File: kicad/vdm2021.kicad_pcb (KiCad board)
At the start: 2 copper layers, 254 x 134.1 mm, 177 parts, among them IC1 7406, IC10 74LS109, IC11 74LS138, IC12 74LS86, IC13 74LS109, IC14 74LS02, IC15 74LS00, IC16 74LS109, IC17 74LS175, IC18 74LS132, IC19 74LS04, IC2 74LS163, IC20 74LS163, IC21 74LS163, IC22 74LS163, IC23 74LS157, IC24 74LS157, IC25 4049, IC26 4029, IC27 4029, IC28 74LS157, IC29 DM8131, IC3 74166, IC30 4001, IC31 4042, IC32 4042, IC33 74LS08, IC34 74LS08, IC35 74LS00, IC36 74LS04, IC37 8836, IC38 74LS367, IC39 74LS367, IC4 MCM6575, IC40 74LS10, IC41 2102, IC42 2102, IC43 2102, IC44 2102, IC45 2102, IC46 2102, IC47 2102, IC48 2102, IC49 L7805, IC5 74LS175, IC50 L7812, IC6 74LS175, IC7 74LS20, IC8 93L16, IC9 74LS10, J2 Jumper_3_Open, J4 Jumper_2_Open, J5 Jumper_2_Open, Q1 2N2907, SW1 SW_DIP_x06, Y1 Crystal

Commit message: Cleanup structure
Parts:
- ADDR1: footprint vdm2:ADDR_SELECT -> vdm2021:ADDR_SELECT
- HEAT: footprint vdm2:heatsink -> vdm2021:heatsink
- IC49: footprint vdm2:TO-220-3_Horizontal_TabDown -> vdm2021:TO-220-3_Horizontal_TabDown
- S100: footprint vdm2:S100_MALE -> vdm2021:S100_MALE
- VIDEO1: footprint vdm2:bnc-5-16345033 -> vdm2021:bnc-5-16345033
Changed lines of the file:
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@@
       (drillshape 0)
       (scaleselection 1)
-      (outputdirectory "/home/rob/Downloads/vdm2021"))
+      (outputdirectory ""))
   )
   (net 0 "")
@@
     (add_net "Net-(S100-Pad9)")
   )
-  (module vdm2:S100_MALE (layer F.Cu)
+  (module vdm2021:S100_MALE (layer F.Cu)
     (at 55.4482 151.9936)
     (descr "Connecteur Bus PC 8 bits")
@@
     )
   )
-  (module vdm2:TO-220-3_Horizontal_TabDown (layer F.Cu)
+  (module vdm2021:TO-220-3_Horizontal_TabDown (layer F.Cu)
     (at 47.625 58.57)
     (descr "TO-220-3, Horizontal, RM 2.54mm, see https://www.vishay.com/docs/66542/to-220-1.pdf")
@@
     )
   )
-  (module vdm2:bnc-5-16345033 locked (layer F.Cu)
+  (module vdm2021:bnc-5-16345033 locked (layer F.Cu)
     (at 261.62 34.925 270)
     (descr 5-1634503-3-1)
@@
     )
   )
-  (module vdm2:heatsink (layer F.Cu)
+  (module vdm2021:heatsink (layer F.Cu)
     (at 50.165 36.945)
     (fp_text reference HEAT (at 0 0.5) (layer F.SilkS) hide
@@
     )
   )
-  (module vdm2:ADDR_SELECT (layer F.Cu)
+  (module vdm2021:ADDR_SELECT (layer F.Cu)
     (at 101.219 117.094)
     (fp_text reference ADDR1 (at 0.7874 -4.0894) (layer F.SilkS) hide

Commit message: Routing updates after last schematic change
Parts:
- moved R46 3.79 mm to (145.1, 117.0)
- moved C41 0.90 mm to (200.3, 99.1)
- moved C11 0.08 mm to (142.0, 117.0)
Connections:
- IC29 pad 9: Net-(ADDR1-Pad13) -> Net-(IC29-Pad9)
- IC36 pad 3: Net-(ADDR1-Pad13) -> Net-(IC29-Pad9)
- IC37 pad 5: Net-(ADDR1-Pad13) -> Net-(IC29-Pad9)
- IC38 pad 15: Net-(ADDR1-Pad13) -> Net-(IC29-Pad9)
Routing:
- net Net-(IC31-Pad4): track 366.2 -> 180.4 mm, vias 6 -> 3
- net Net-(IC29-Pad9): track 0.00 -> 120.4 mm, vias 0 -> 2
- net Net-(ADDR1-Pad13): track 229.8 -> 284.0 mm
- net Net-(ADDR1-Pad10): track 153.9 -> 133.0 mm, vias 3 -> 2
- net Net-(IC32-Pad13): track 243.4 -> 222.9 mm
- net +5V: track 1752.7 -> 1743.2 mm
- net Net-(IC36-Pad1): track 92.7 -> 99.6 mm, vias 3 -> 2
- net Net-(IC38-Pad5): track 43.5 -> 49.8 mm, vias 2 -> 3
- net Net-(IC29-Pad13): track 61.6 -> 67.1 mm
- net Net-(IC29-Pad3): track 76.4 -> 81.7 mm
- net Net-(IC29-Pad5): track 75.7 -> 80.8 mm
- net Net-(IC28-Pad6): track 116.7 -> 112.9 mm
- net Net-(IC33-Pad5): track 59.6 -> 63.3 mm
- net Net-(IC36-Pad8): track 114.8 -> 117.8 mm, vias 1 -> 2
- net Net-(IC34-Pad1): track 78.0 -> 75.4 mm
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
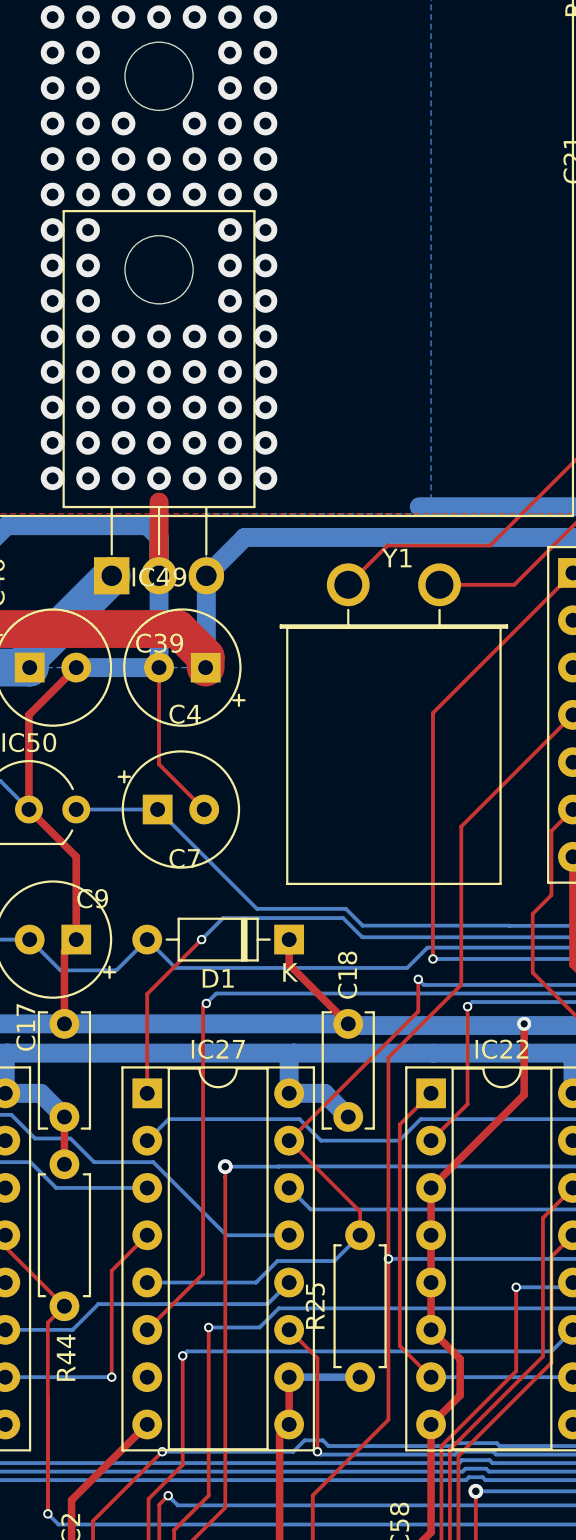
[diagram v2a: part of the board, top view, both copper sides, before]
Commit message: Fixed IC22 load value
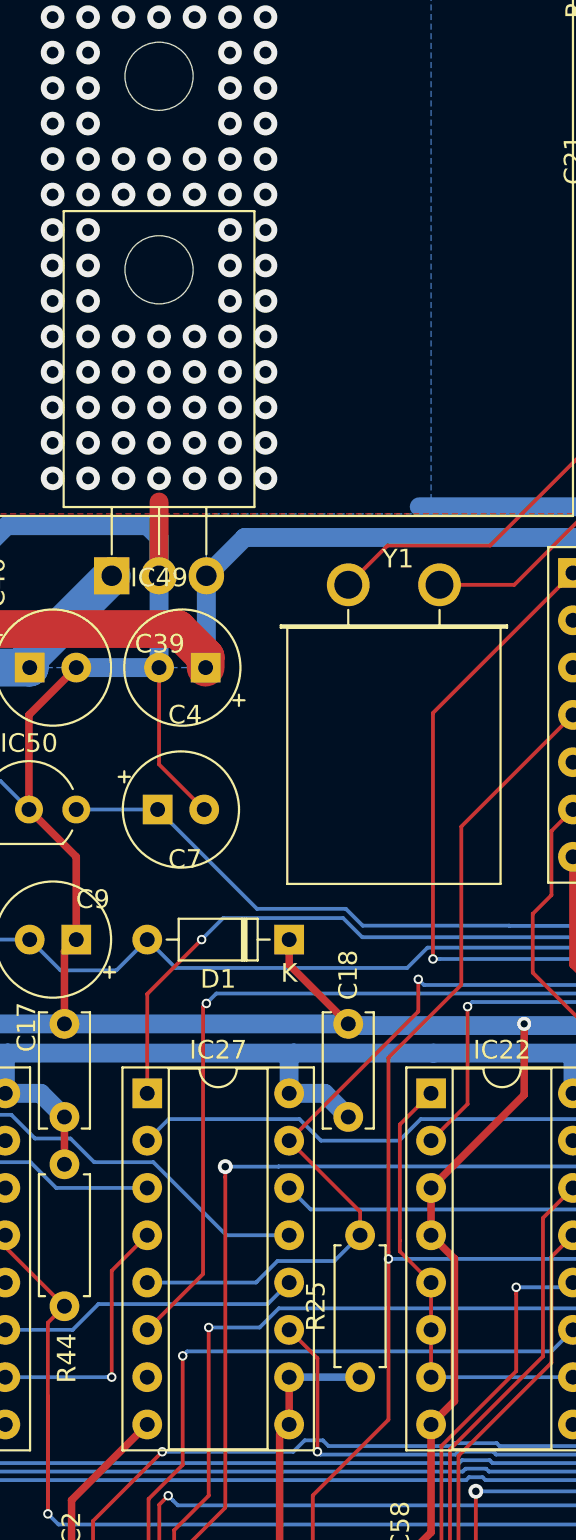
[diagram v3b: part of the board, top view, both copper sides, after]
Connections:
- IC22 pad 5: GND -> Net-(IC20-Pad1)
- IC22 pad 6: GND -> Net-(IC20-Pad1)
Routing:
- net GND: track 2507.7 -> 2507.5 mm, vias 142 -> 140

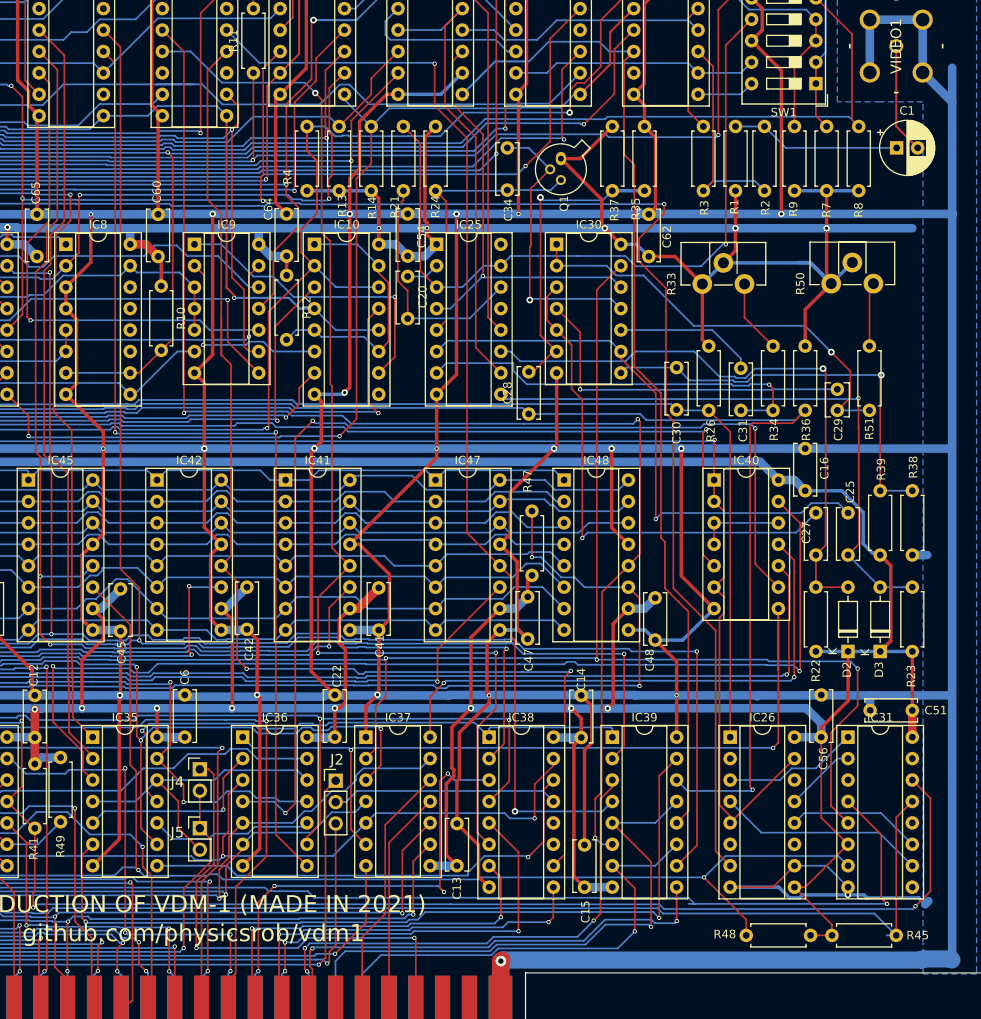
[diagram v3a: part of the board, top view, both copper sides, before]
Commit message: Fixed IC39 Gnd/pwr swap
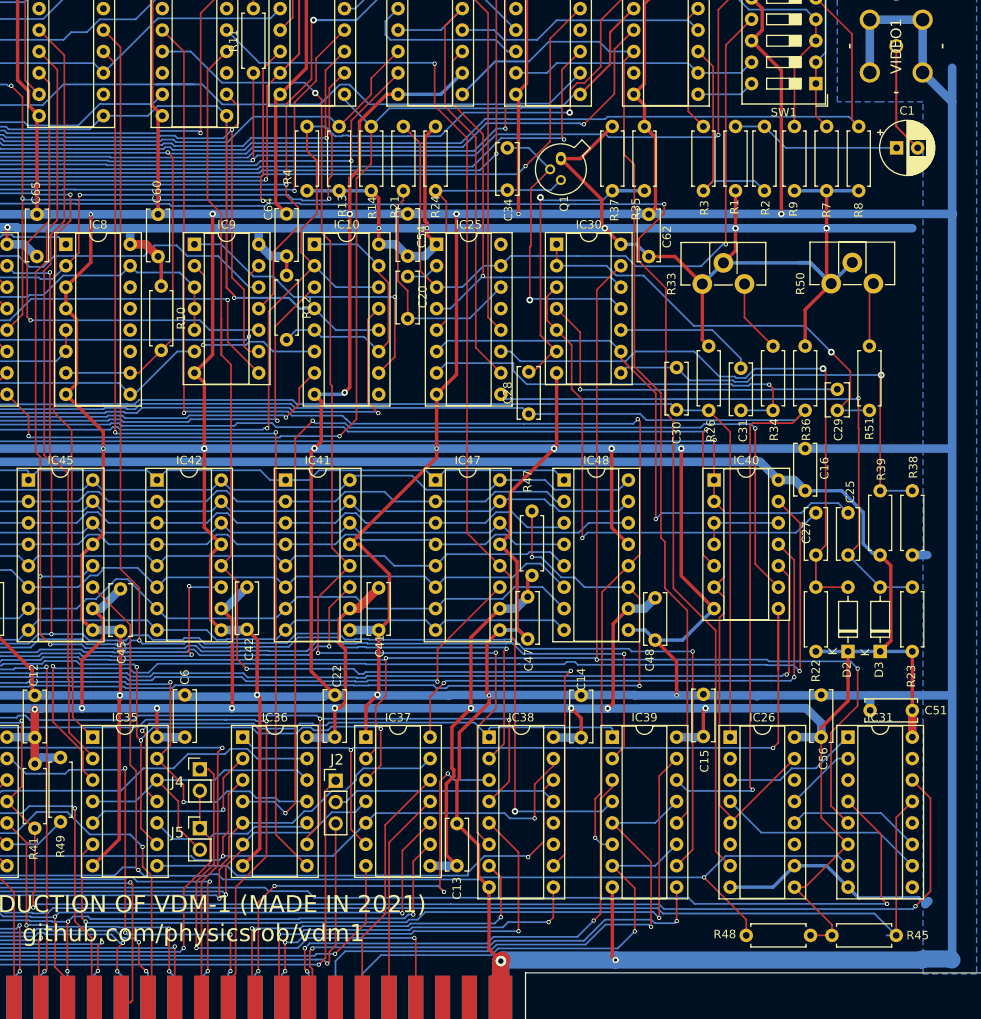
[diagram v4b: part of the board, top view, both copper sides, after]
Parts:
- moved C15 22.8 mm to (238.8, 116.8)
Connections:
- IC39 pad 16: GND -> +5V
- IC39 pad 8: +5V -> GND
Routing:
- net GND: track 2507.5 -> 2486.8 mm
- net +5V: track 1743.2 -> 1727.9 mm, vias 26 -> 27
- net Net-(IC31-Pad4): track 180.4 -> 179.7 mm
- net Net-(IC39-Pad10): track 237.8 -> 237.1 mm

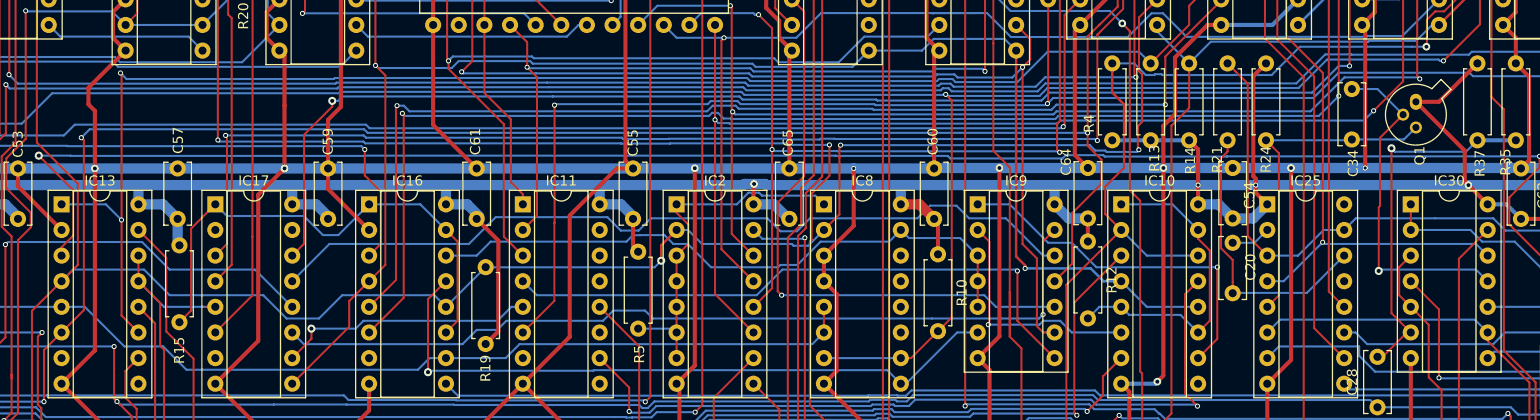
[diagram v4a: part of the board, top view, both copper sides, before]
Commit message: Fix Q1 pinout
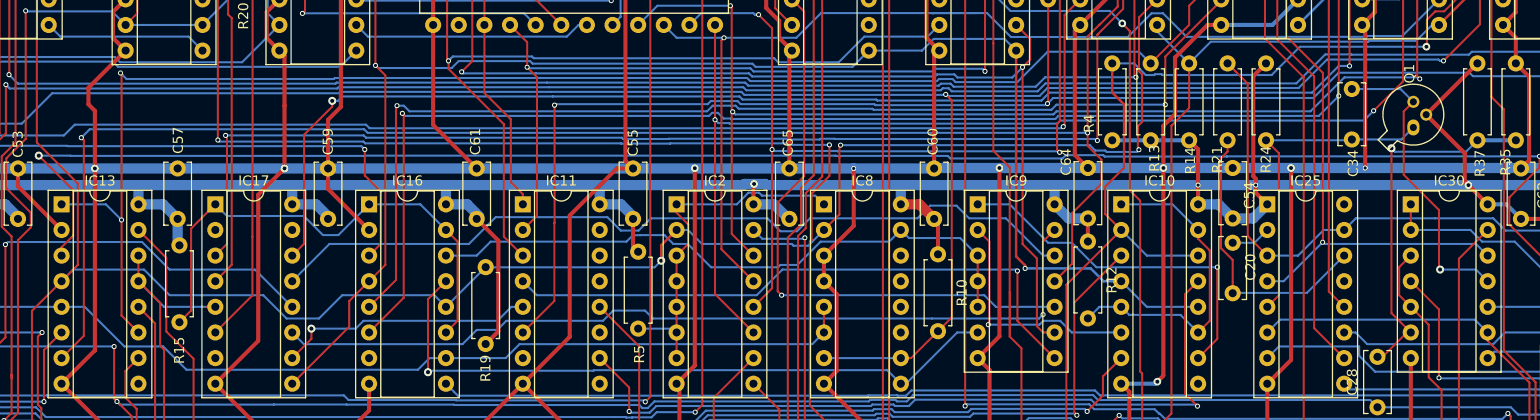
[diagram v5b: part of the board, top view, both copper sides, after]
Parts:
- moved Q1 2.55 mm to (221.6, 50.8), turned to 90 degrees
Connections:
- IC7 pad 4: Net-(IC13-Pad6) -> Net-(IC13-Pad7)
- IC9 pad 11: Net-(IC13-Pad6) -> Net-(IC13-Pad7)
- Q1 pad 1: +5V -> Net-(C34-Pad2)
- Q1 pad 2: Net-(C34-Pad1) -> +5V
- Q1 pad 3: Net-(C34-Pad2) -> Net-(C34-Pad1)
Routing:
- net Net-(IC13-Pad7): track 0.00 -> 187.8 mm, vias 0 -> 3
- net Net-(IC13-Pad6): track 236.6 -> 51.4 mm, vias 5 -> 2
- net Net-(C34-Pad1): track 34.0 -> 30.3 mm
- net +5V: track 1727.9 -> 1725.7 mm

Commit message: Silkscreen tweaks
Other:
- board text added: "GND"
- board text added: "X"
- board text added: "Y"

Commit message: Misc PCB
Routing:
- net Net-(IC27-Pad2): track 73.0 -> 69.9 mm
- net Net-(IC31-Pad4): track 179.7 -> 177.8 mm
- net Net-(IC37-Pad7): track 71.2 -> 73.0 mm
- net Net-(IC38-Pad3): track 55.6 -> 54.2 mm
- net Net-(IC31-Pad14): track 202.2 -> 200.8 mm
- net Net-(IC29-Pad5): track 80.8 -> 79.7 mm
- net Net-(IC31-Pad13): track 192.4 -> 191.4 mm
- net Net-(IC39-Pad13): track 67.1 -> 66.1 mm
- net Net-(J2-Pad1): track 94.4 -> 95.4 mm
- net Net-(IC35-Pad6): track 98.5 -> 97.5 mm
- net Net-(IC28-Pad3): track 123.0 -> 122.1 mm
- net Net-(IC23-Pad10): track 114.5 -> 113.8 mm
- net Net-(IC38-Pad2): track 149.2 -> 149.9 mm
- net Net-(IC23-Pad3): track 135.9 -> 135.2 mm
- net Net-(IC33-Pad5): track 63.3 -> 62.8 mm
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
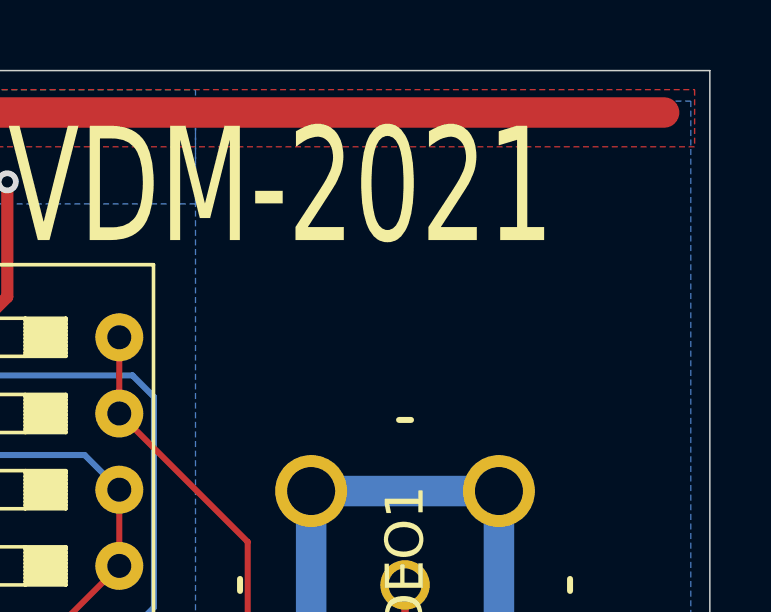
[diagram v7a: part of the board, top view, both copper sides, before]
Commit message: Added rev silkscreen
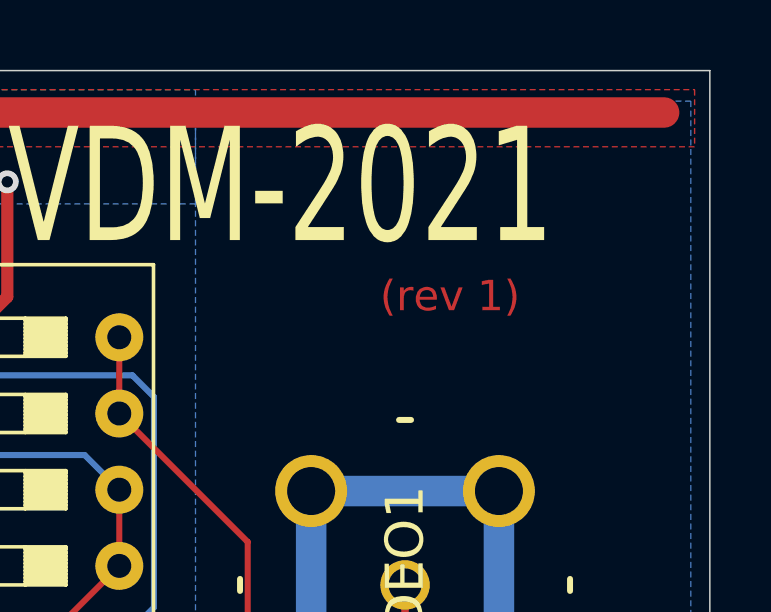
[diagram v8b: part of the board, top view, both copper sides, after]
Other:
- board text added: "(rev 1)"
